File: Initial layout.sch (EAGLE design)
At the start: 55 parts, among them J1 502585-0470, U2 TPS54540DDARQ1

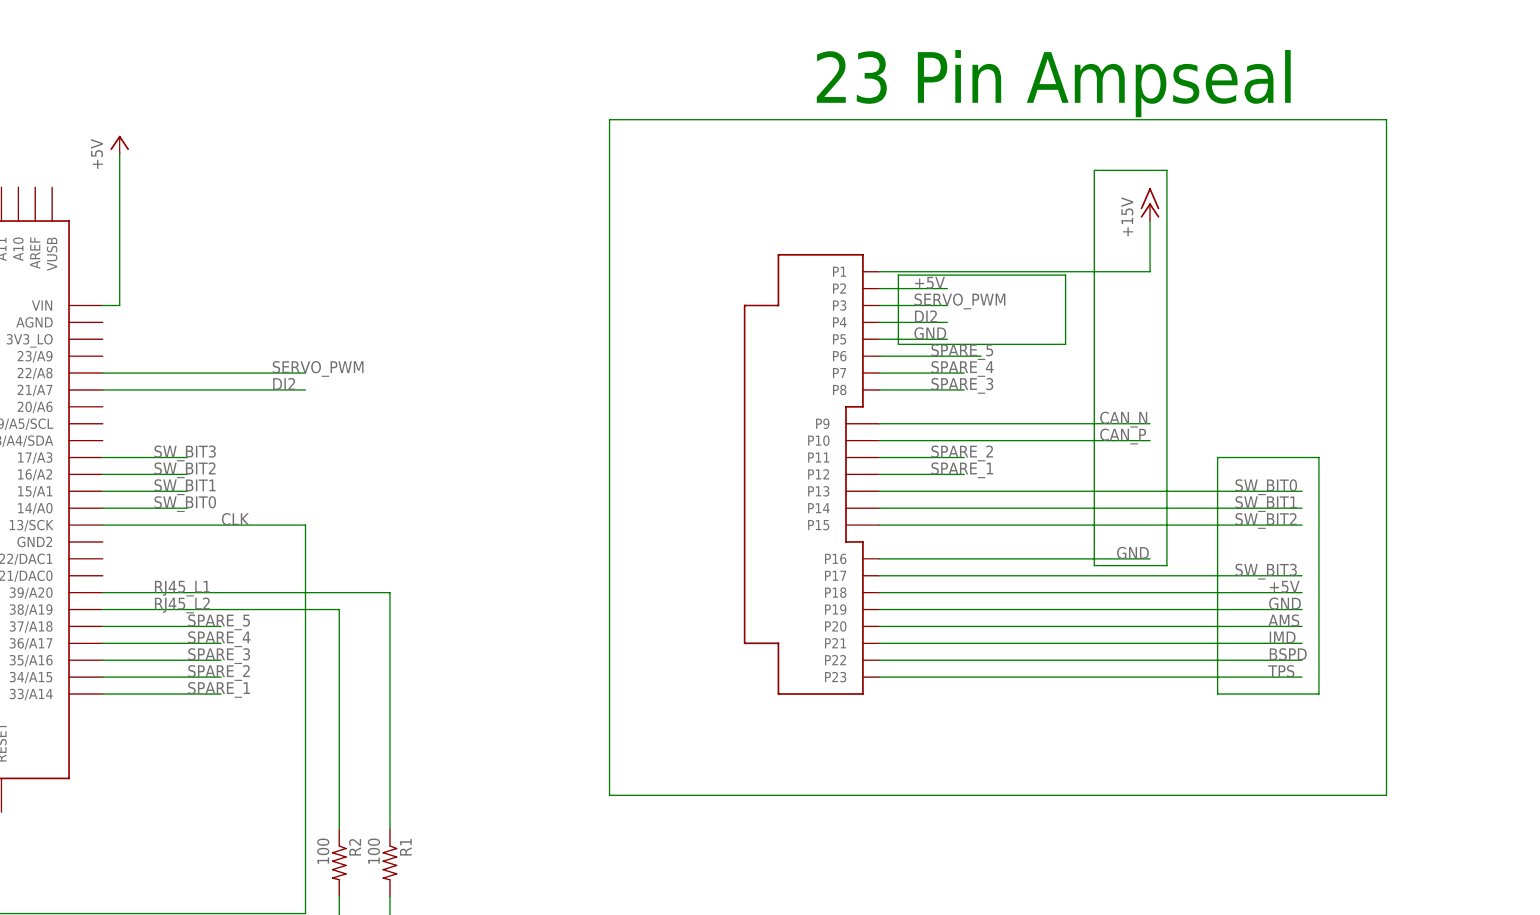
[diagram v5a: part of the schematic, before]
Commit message: Updated Schematic
*Warning* The board did not update with the schematic
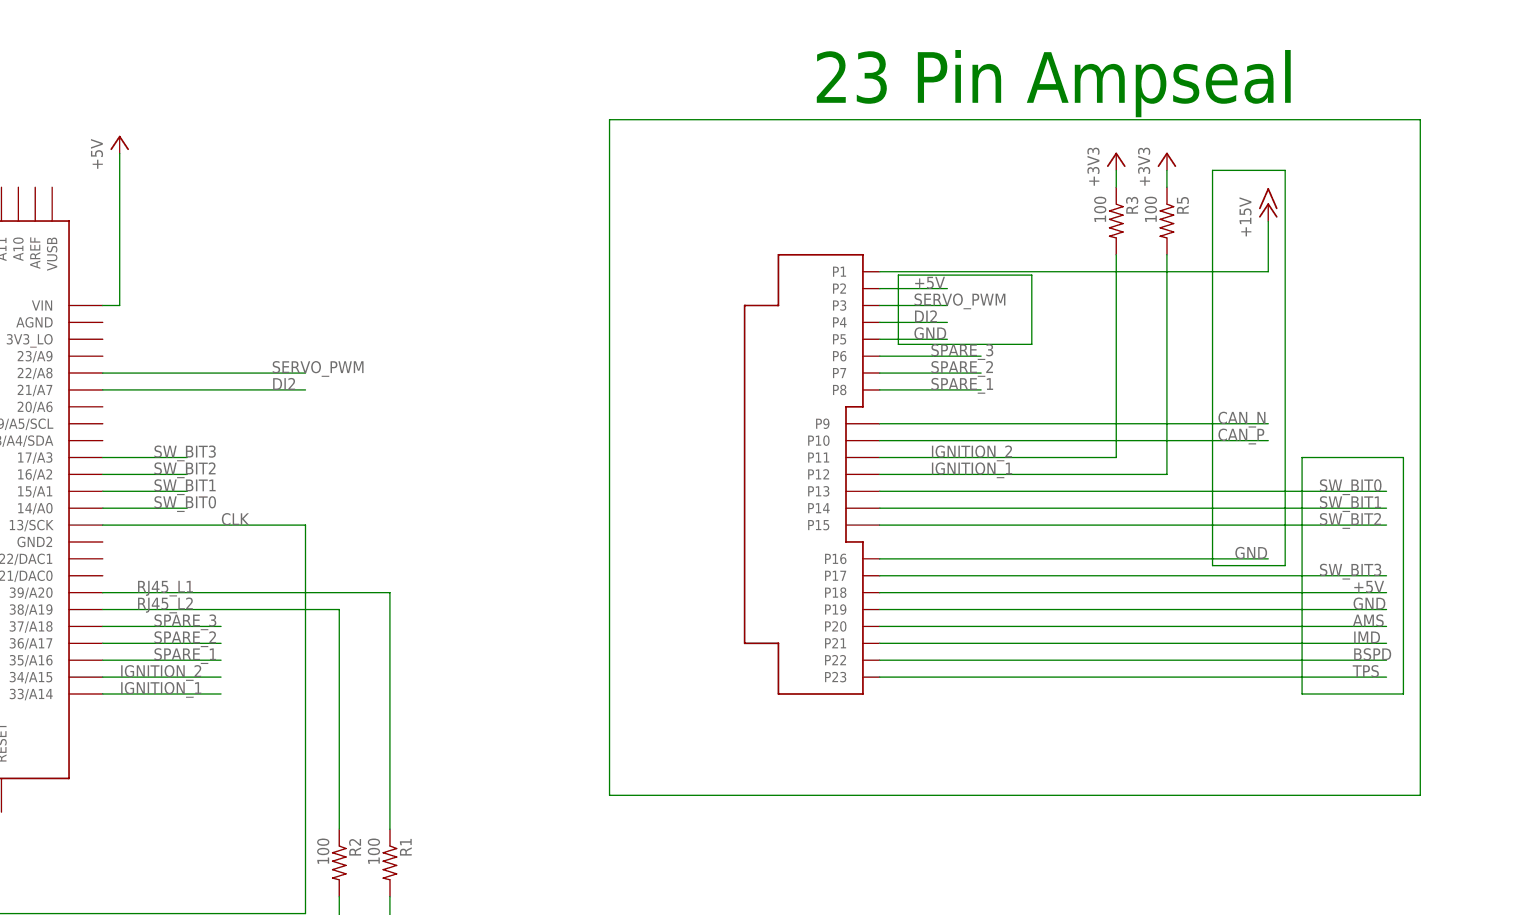
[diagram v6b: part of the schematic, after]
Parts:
- added R3, R5: 100, rcl:R-US_R0805
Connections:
- removed net SPARE_4: U$1.P7, U$2.36/A17
- removed net SPARE_5: U$1.P6, U$2.37/A18
- new net +1V2: R3.1, R5.1
- new net IGNITION_1: R5.2, U$1.P12, U$2.33/A14
- new net IGNITION_2: R3.2, U$1.P11, U$2.34/A15
- net SPARE_1: now also U$1.P8, U$2.35/A16; no longer U$1.P12, U$2.33/A14
- net SPARE_2: now also U$1.P7, U$2.36/A17; no longer U$1.P11, U$2.34/A15
- net SPARE_3: now also U$1.P6, U$2.37/A18; no longer U$1.P8, U$2.35/A16
